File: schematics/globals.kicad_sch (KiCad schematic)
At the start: 16 parts, among them J1 Power, SW4 SW_Push, U21 NE555P, Y1 4MHz

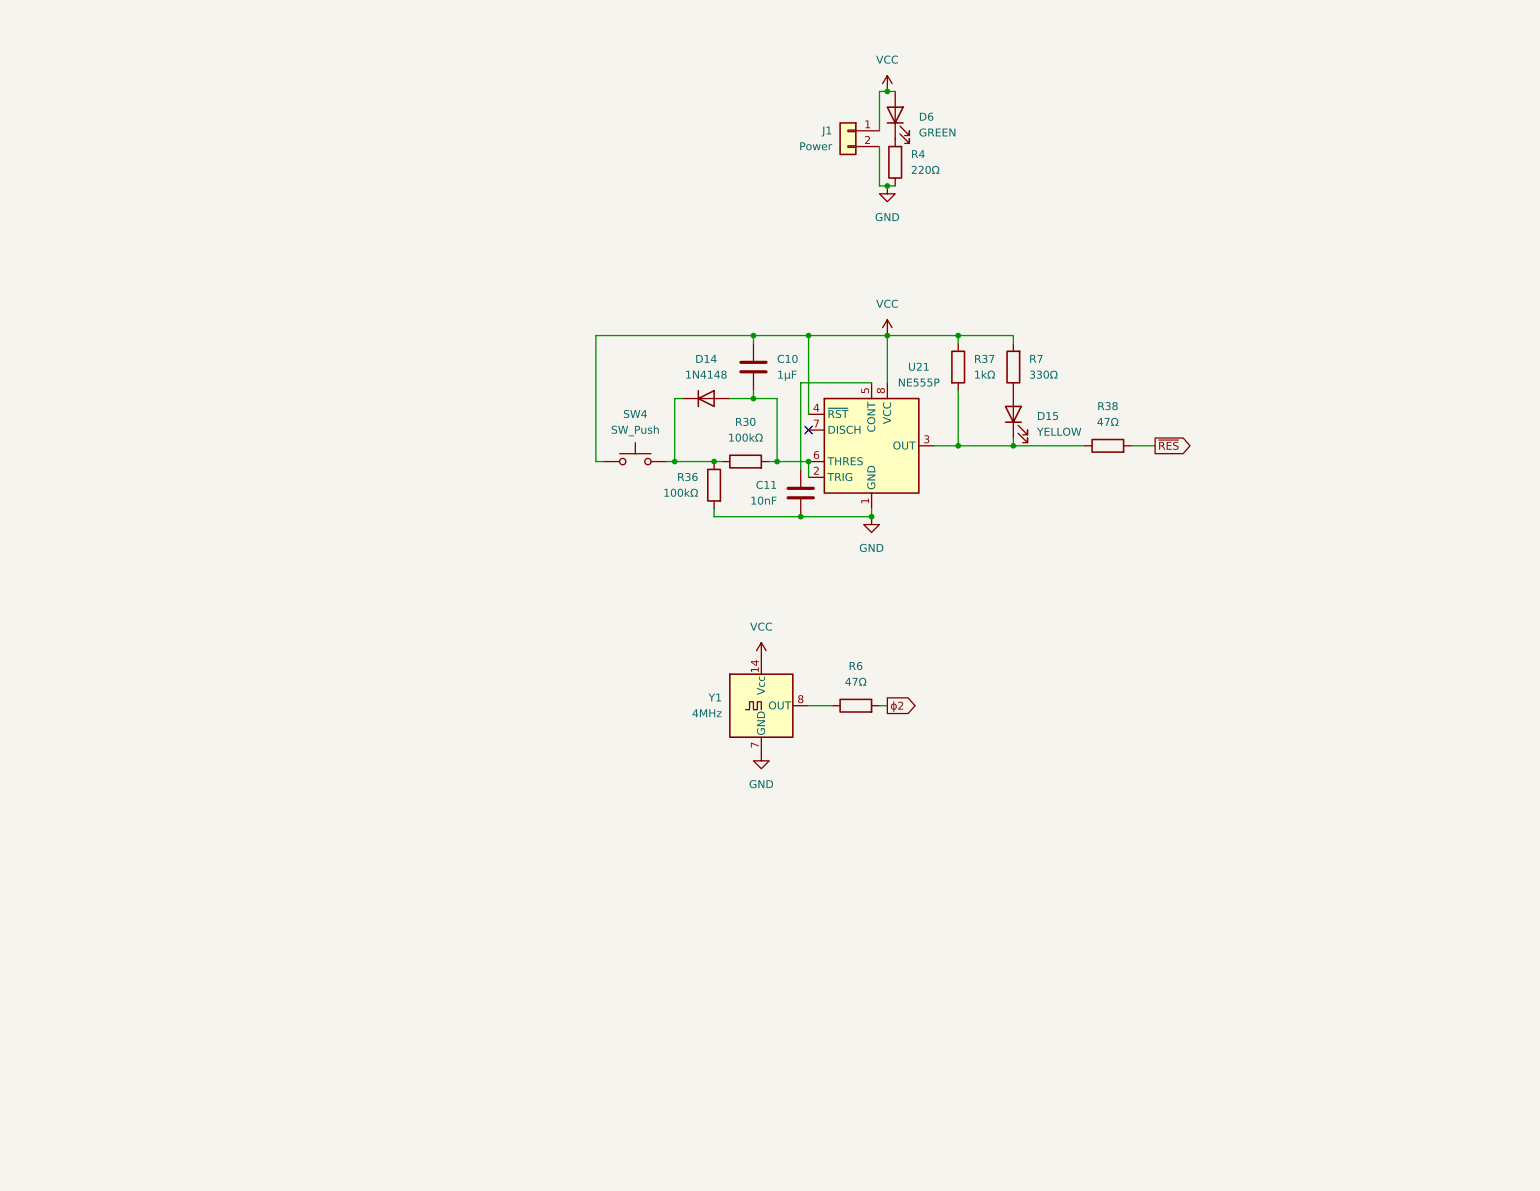
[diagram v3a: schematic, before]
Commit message: PLD files and schematics for address decoder, device selector, keyboard controller, lcd controller, banked memory, and bootloader.
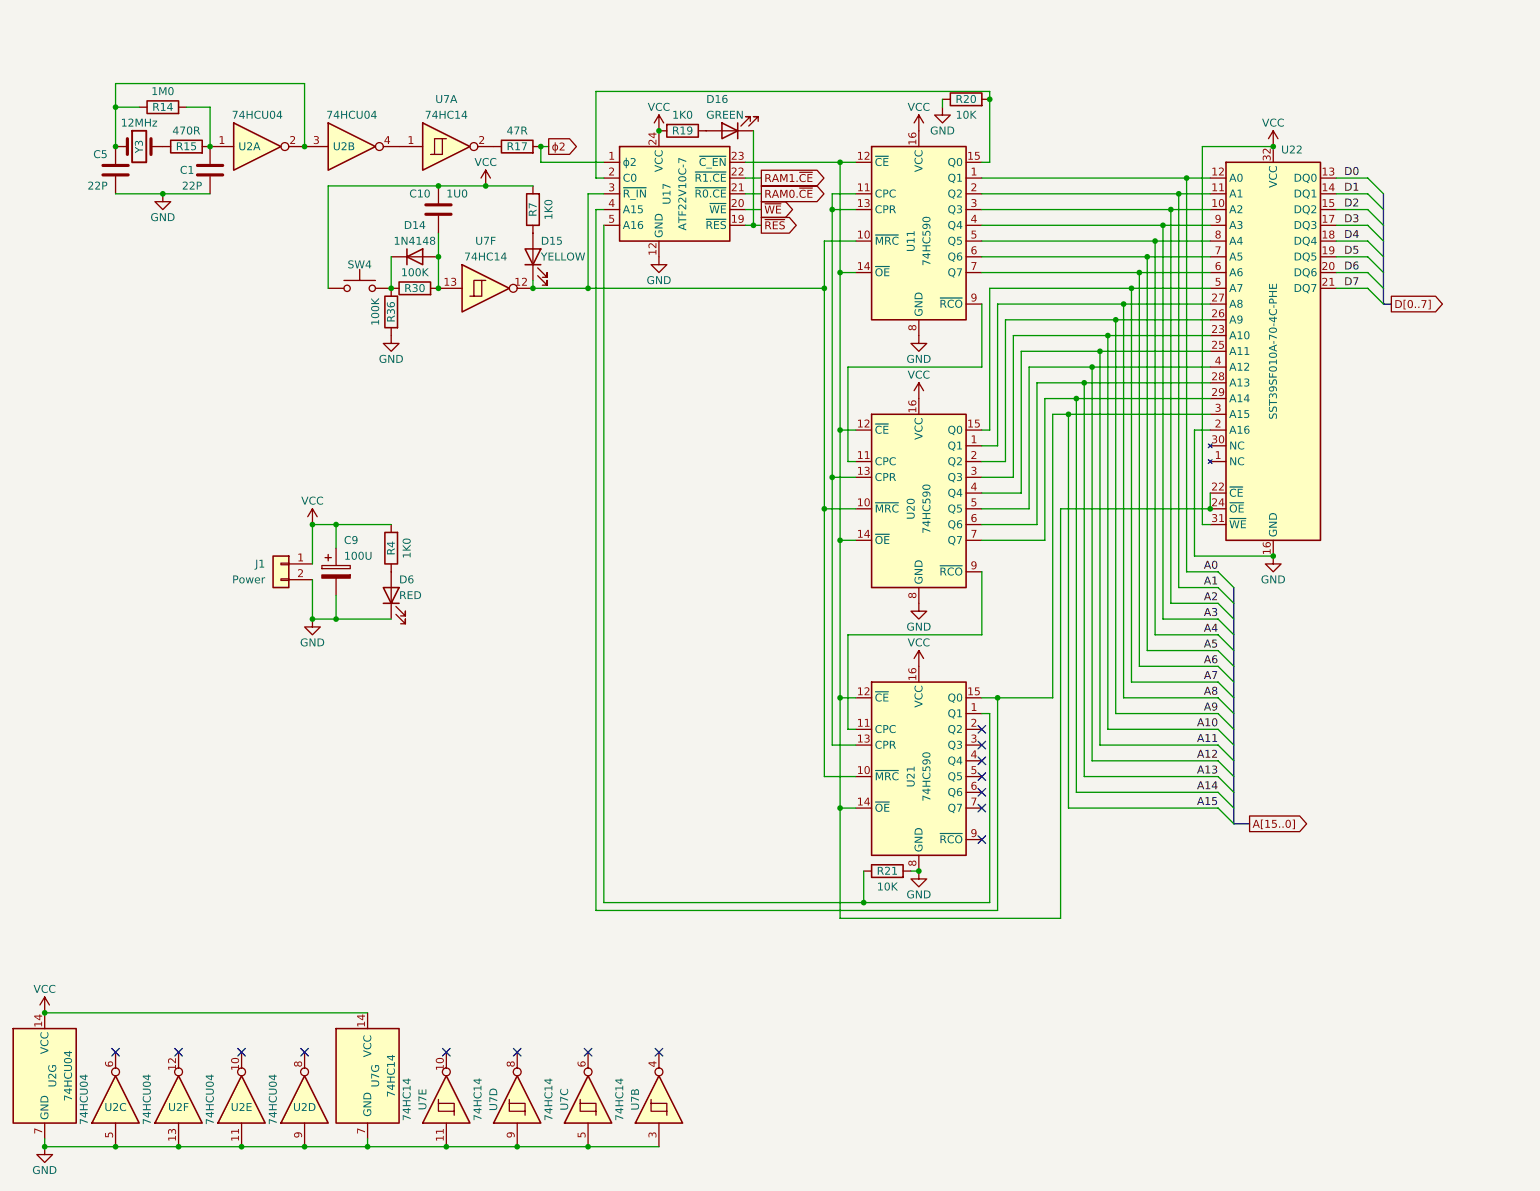
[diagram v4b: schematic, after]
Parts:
- removed C11: 10nF, symbol Device:C
- removed R37: 1kΩ, symbol Device:R
- removed R38, R6: 47Ω, symbol Device:R
- removed U21: NE555P, Package_DIP:DIP-8_W7.62mm, symbol Timer:NE555P
- removed Y1: 4MHz, Oscillator:Oscillator_DIP-14, symbol Oscillator:DGOF5S3
- added C1, C5: 22P, symbol Device:C
- added C9: 100U, symbol Device:C_Polarized
- added D16: GREEN, symbol Device:LED
- added R14: 1M0, symbol Device:R
- added R15: 470R, symbol Device:R
- added R17: 47R, symbol Device:R
- added R19: 1K0, symbol Device:R
- added R20, R21: 10K, symbol Device:R
- added U11, U20, U21: 74HC590, symbol 74xx:74HC590
- added U17: ATF22V10C-7, Package_DIP:DIP-24_W7.62mm, symbol Logic_Programmable:PEEL22CV10AP
- added U2: 74HCU04, symbol 74xx:74HC04
- added U22: SST39SF010A-70-4C-PHE, symbol Memory_Flash:SST39SF010
- added U7: 74HC14, symbol 74xx:74HC14
- added Y3: 12MHz, symbol Device:Crystal
- C10: value 1µF -> 1U0
- D6: value GREEN -> RED
- R30, R36: value 100kΩ -> 100K
- R4: value 220Ω -> 1K0
- R7: value 330Ω -> 1K0
- SW4: value SW_Push -> (none)
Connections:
- net GND: now also D6.1 (K), C1.2, C5.2, C9.2, R20.1, R21.2, U11.8 (GND), U17.12 (GND), U2.11, U2.13, U2.5, U2.7 (GND), U2.9, U20.8 (GND), U21.8 (GND), U22.16 (GND), U22.2 (A16), U7.11, U7.3, U7.5, U7.7 (GND), U7.9; no longer R4.1
- net VCC: now also R4.2, C9.1, R19.2, U11.16 (VCC), U17.24 (VCC), U2.14 (VCC), U20.16 (VCC), U21.16 (VCC), U22.31 (~{WE}), U22.32 (VCC), U7.14 (VCC); no longer D6.2 (A)
- net ~{RES}: now also D16.1 (K), U17.19 (~{RES})
- net ϕ2: now also R17.2, U17.1 (ϕ2)
- net at C10.1, D14.2 (A), R30.2: now also U7.13
- net at D15.1 (K): now also U11.10 (~{MRC}), U17.3 (~{R_IN}), U20.10 (~{MRC}), U21.10 (~{MRC}), U7.12
- new net: U11.11 (CPC), U11.13 (CPR), U20.13 (CPR), U21.13 (CPR)
- new net: U11.12 (~{CE}), U11.14 (~{OE}), U17.23 (~{C_EN}), U20.12 (~{CE}), U20.14 (~{OE}), U21.12 (~{CE}), U21.14 (~{OE}), U22.22 (~{CE}), U22.24 (~{OE})
- new net: R20.2, U11.15 (Q0), U17.2 (C0)
- new net: U11.9 (~{RCO}), U20.11 (CPC)
- new net: C5.1, R14.1, U2.2, U2.3, Y3.1
- new net: U2.4, U7.1
- new net: D6.2 (A), R4.1
- new net: C1.1, R14.2, R15.2, U2.1
- new net: R21.1, U17.5 (A16), U21.1 (Q1)
- new net: U20.9 (~{RCO}), U21.11 (CPC)
- new net: D16.2 (A), R19.1
- new net: R17.1, U7.2
- new net: R15.1, Y3.2
- new net A0: U11.1 (Q1), U22.12 (A0)
- new net A1: U11.2 (Q2), U22.11 (A1)
- new net A10: U20.3 (Q3), U22.23 (A10)
- new net A11: U20.4 (Q4), U22.25 (A11)
- new net A12: U20.5 (Q5), U22.4 (A12)
- new net A13: U20.6 (Q6), U22.28 (A13)
- new net A14: U20.7 (Q7), U22.29 (A14)
- new net A15: U17.4 (A15), U21.15 (Q0), U22.3 (A15)
- new net A2: U11.3 (Q3), U22.10 (A2)
- new net A3: U11.4 (Q4), U22.9 (A3)
- new net A4: U11.5 (Q5), U22.8 (A4)
- new net A5: U11.6 (Q6), U22.7 (A5)
- new net A6: U11.7 (Q7), U22.6 (A6)
- new net A7: U20.15 (Q0), U22.5 (A7)
- new net A8: U20.1 (Q1), U22.27 (A8)
- new net A9: U20.2 (Q2), U22.26 (A9)
- new net D0: U22.13 (DQ0)
- new net D1: U22.14 (DQ1)
- new net D2: U22.15 (DQ2)
- new net D3: U22.17 (DQ3)
- new net D4: U22.18 (DQ4)
- new net D5: U22.19 (DQ5)
- new net D6: U22.20 (DQ6)
- new net D7: U22.21 (DQ7)
- new net RAM0.~{CE}: U17.21 (~{R0.CE})
- new net RAM1.~{CE}: U17.22 (~{R1.CE})
- new net ~{WE}: U17.20 (~{WE})
- no-connect marks 1 -> 15
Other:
- moved on the sheet: C10, D14, D15, D6, J1, R30, R36, R4, R7, SW4

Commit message: added phi0 for write latch timing
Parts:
- added R26: 47R, symbol Device:R
- C1, C5: value 22P -> 20P
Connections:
- net GND: no longer U2.5, U2.9, U7.3
- net at U2.8: now also U7.3
- net at U2.4, U7.1: now also U2.5
- net at U2.6: now also U2.9
- net at U7.2: now also R26.1; no longer R17.1
- net at U7.4: now also R17.1
- new net ϕ0: R26.2
- no-connect marks 15 -> 12
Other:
- note added: "10ns earlier clock to latch writes within 10ns hold time"
- moved on the sheet: C1, C10, C5, C9, D14, D15, D16, D6, J1, R14, R15, R17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

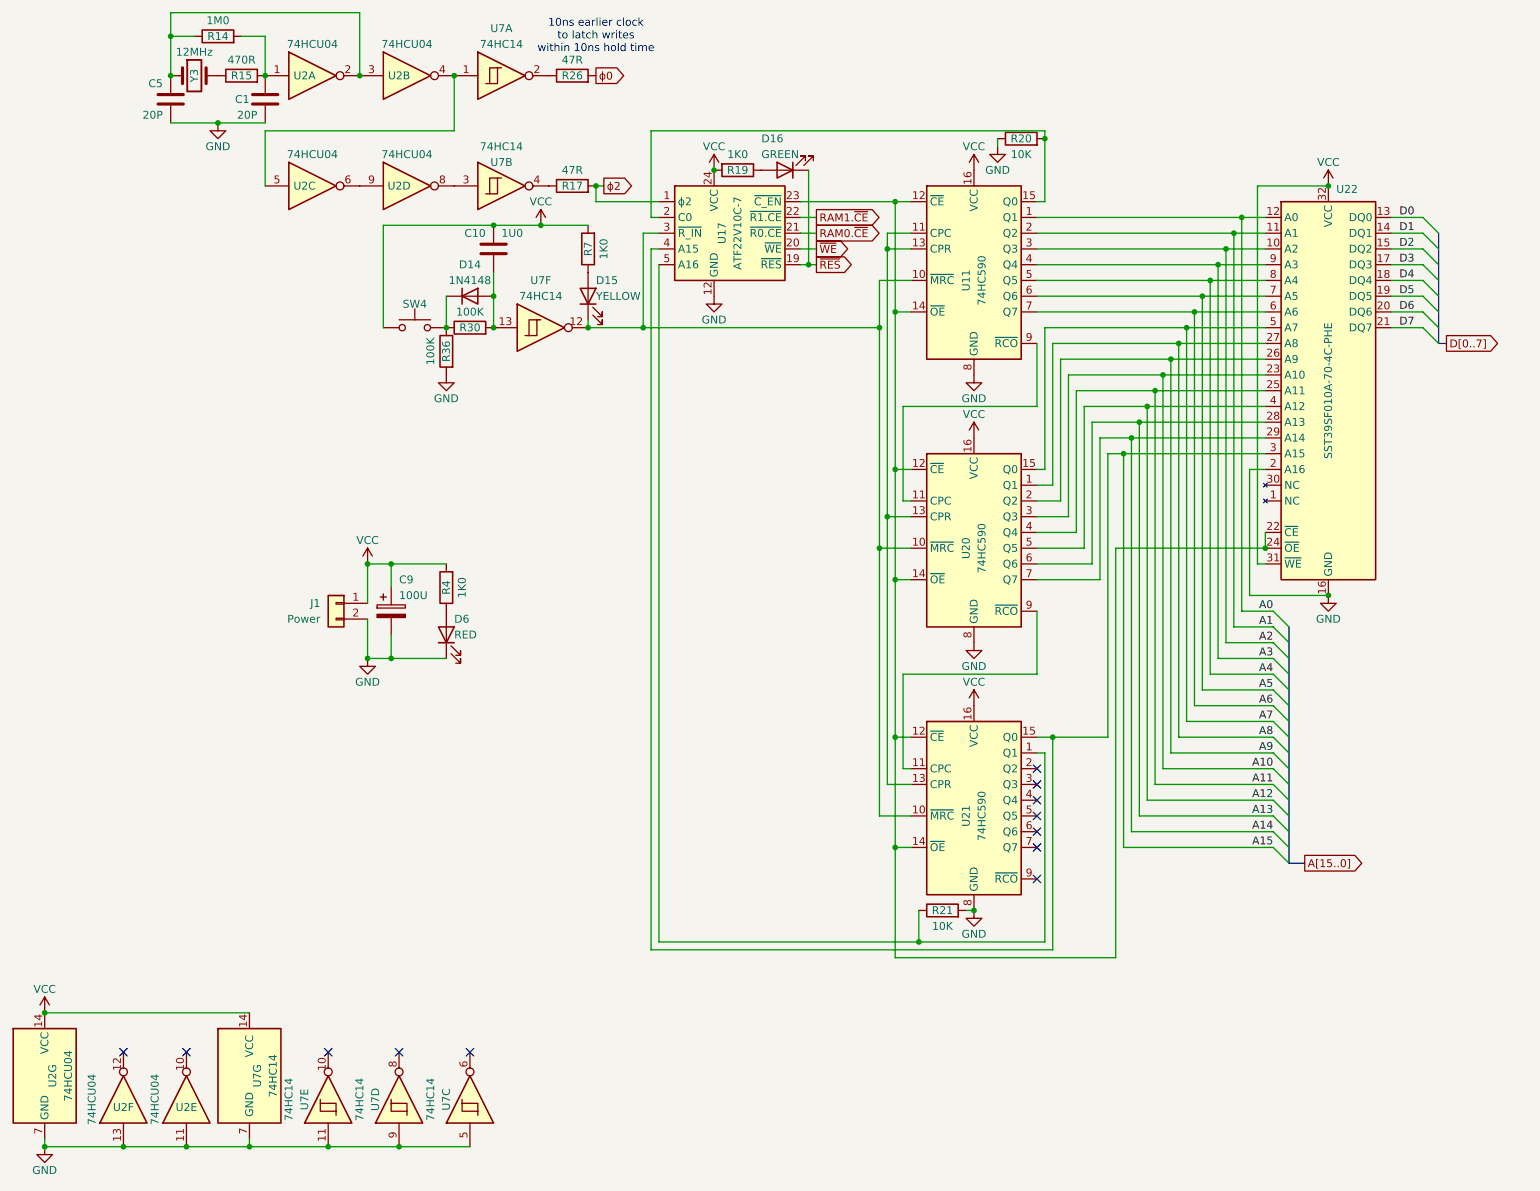
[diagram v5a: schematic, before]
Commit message: fixes to bootloader; finished via schematic
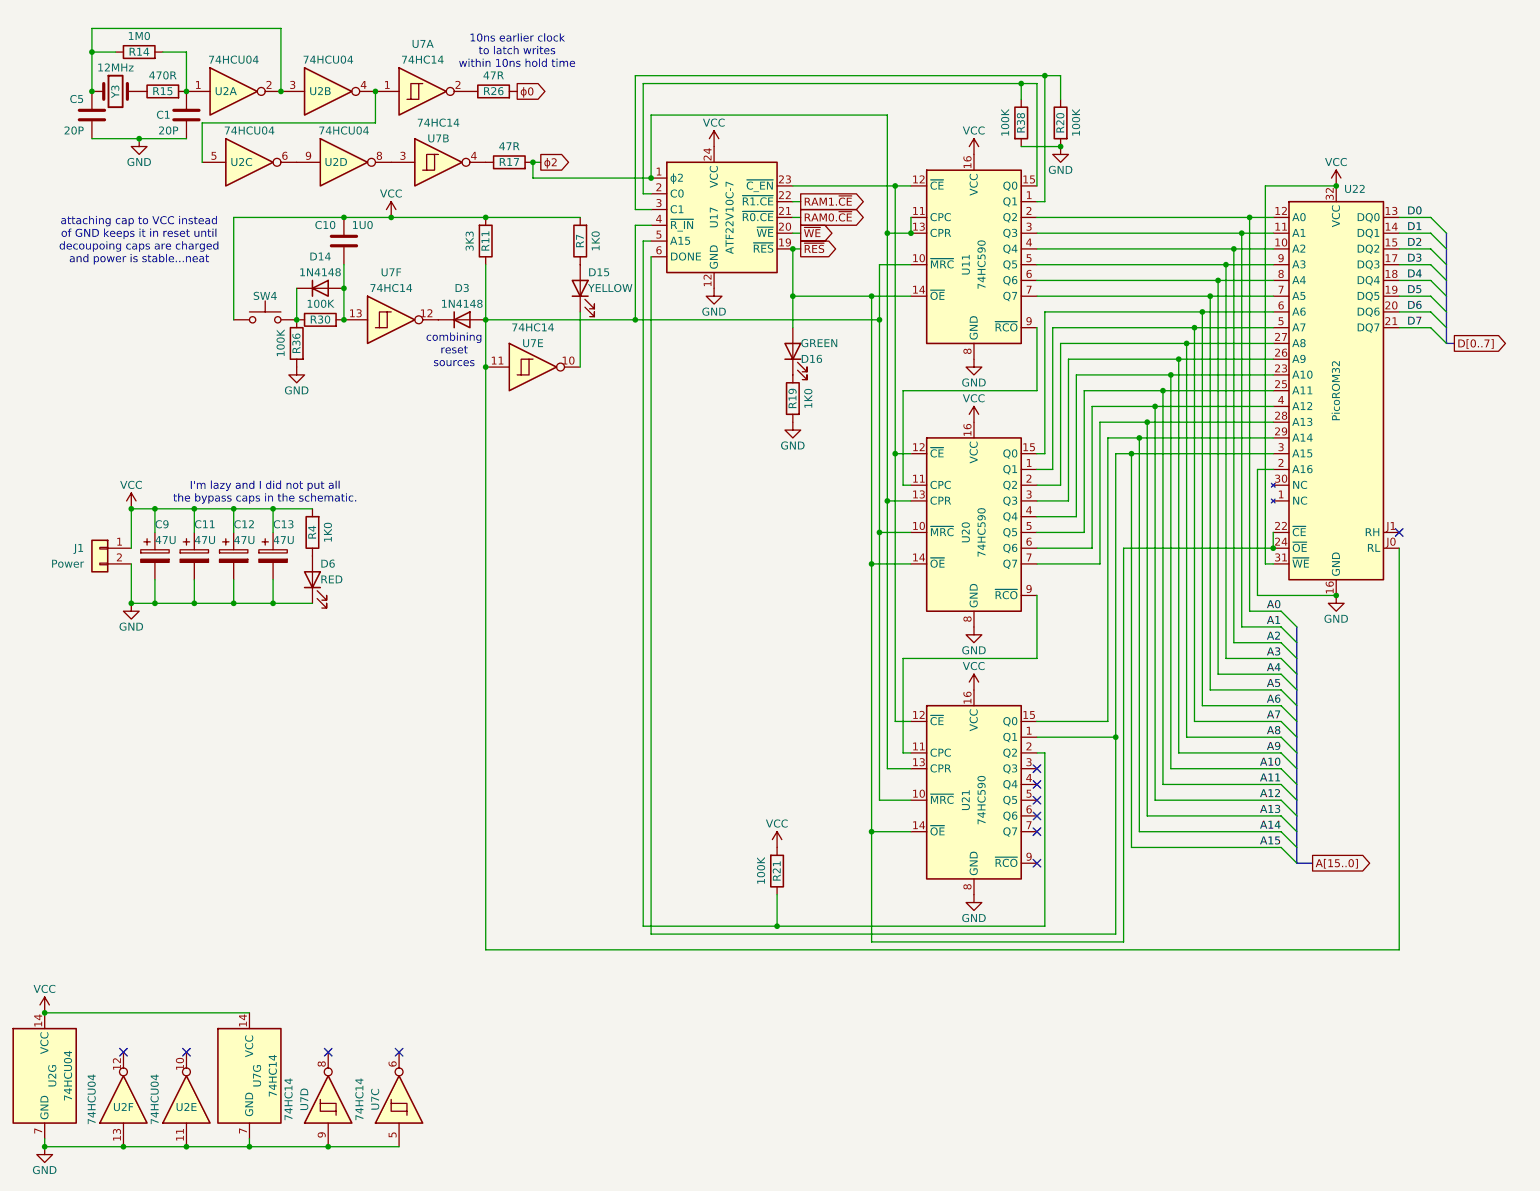
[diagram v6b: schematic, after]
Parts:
- added C11, C12, C13: 47U, symbol Device:C_Polarized
- added D3: 1N4148, Diode_THT:D_DO-35_SOD27_P7.62mm_Horizontal, symbol Diode:1N4148
- added R11: 3K3, symbol Device:R
- added R38: 100K, symbol Device:R
- C9: value 100U -> 47U
- R20, R21: value 10K -> 100K
- U22: value SST39SF010A-70-4C-PHE -> PicoROM32
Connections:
- net A0: now also U11.2 (Q2); no longer U11.1 (Q1)
- net A1: now also U11.3 (Q3); no longer U11.2 (Q2)
- net A10: now also U20.4 (Q4); no longer U20.3 (Q3)
- net A11: now also U20.5 (Q5); no longer U20.4 (Q4)
- net A12: now also U20.6 (Q6); no longer U20.5 (Q5)
- net A13: now also U20.7 (Q7); no longer U20.6 (Q6)
- net A14: now also U21.15 (Q0); no longer U20.7 (Q7)
- net A15: now also U17.6 (DONE), U21.1 (Q1); no longer U17.4 (A15), U21.15 (Q0)
- net A2: now also U11.4 (Q4); no longer U11.3 (Q3)
- net A3: now also U11.5 (Q5); no longer U11.4 (Q4)
- net A4: now also U11.6 (Q6); no longer U11.5 (Q5)
- net A5: now also U11.7 (Q7); no longer U11.6 (Q6)
- net A6: now also U20.15 (Q0); no longer U11.7 (Q7)
- net A7: now also U20.1 (Q1); no longer U20.15 (Q0)
- net A8: now also U20.2 (Q2); no longer U20.1 (Q1)
- net A9: now also U20.3 (Q3); no longer U20.2 (Q2)
- net GND: now also R19.2, R20.2, C11.2, C12.2, C13.2, R38.2; no longer R20.1, R21.2, U7.11
- net VCC: now also R21.2, C11.1, C12.1, C13.1, R11.2; no longer R19.2
- net ~{RES}: now also D16.2 (A), U11.14 (~{OE}), U20.14 (~{OE}), U21.14 (~{OE}), U22.22 (~{CE}), U22.24 (~{OE}); no longer D16.1 (K)
- net ϕ2: now also U11.11 (CPC), U11.13 (CPR), U20.13 (CPR), U21.13 (CPR)
- net at U11.10 (~{MRC}), U20.10 (~{MRC}), U21.10 (~{MRC}): now also U17.4 (~{R_IN}), U22.J0 (RL), U7.11, D3.2 (A), R11.1; no longer D15.1 (K), U17.3 (~{R_IN}), U7.12
- net at U11.15 (Q0), U17.2 (C0): now also R38.1; no longer R20.2
- net at R21.1, U17.5 (A15): now also U21.2 (Q2); no longer U21.1 (Q1)
- net at R19.1: now also D16.1 (K); no longer D16.2 (A)
- net at U7.10: now also D15.1 (K)
- new net: R20.1, U11.1 (Q1), U17.3 (C1)
- new net: U11.12 (~{CE}), U17.23 (~{C_EN}), U20.12 (~{CE}), U21.12 (~{CE})
- new net: D3.1 (K), U7.12
- no-connect marks 12 -> 11
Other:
- note added: "I'm lazy and I did not put all the bypass caps in the schematic."
- note added: "attaching cap to VCC instead of GND keeps it in reset until decoupoing caps are charged and power is stable...neat"
- note added: "combining reset sources"
- moved on the sheet: C1, C10, C5, C9, D14, D6, J1, R14, R15, R17, R20, R21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

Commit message: updating schematics as I wire the board
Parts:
- renumbered C5 to C1, C9 to C2, C1 to C3, C11 to C4, C12 to C5, C13 to C6, C10 to C7, D6 to D1, D14 to D2, D15 to D4, D16 to D5, R14 to R1, R21 to R10, R19 to R11, R38 to R12, R20 to R13, R15 to R2, R36 to R3, R30 to R5, R11 to R6, R26 to R7, R17 to R8, R7 to R9, SW4 to SW1, U2 to U1, U7 to U2, U17 to U3, U11 to U4, U20 to U5, U21 to U6, U22 to U7, Y3 to Y1
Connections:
- net GND: now also U2.3; no longer U2.9
- net at U1.8: now also U2.13; no longer U2.3
- net at C7.1, D2.2 (A), R5.2: now also U2.9; no longer U2.13
- net at D3.1 (K): now also U2.8; no longer U2.12
- net at C1.1, R1.1, Y1.1: now also R2.1; no longer U1.2, U1.3
- net at C3.1, R1.2, U1.1: now also Y1.2; no longer R2.2
- net at R8.1: now also U2.12; no longer U2.4
- new net: R2.2, U1.2, U1.3
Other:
- moved on the sheet: C1, C3, R1, R2, Y1
